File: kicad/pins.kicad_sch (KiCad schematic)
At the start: 2 parts, among them J1 Left, J2 Right

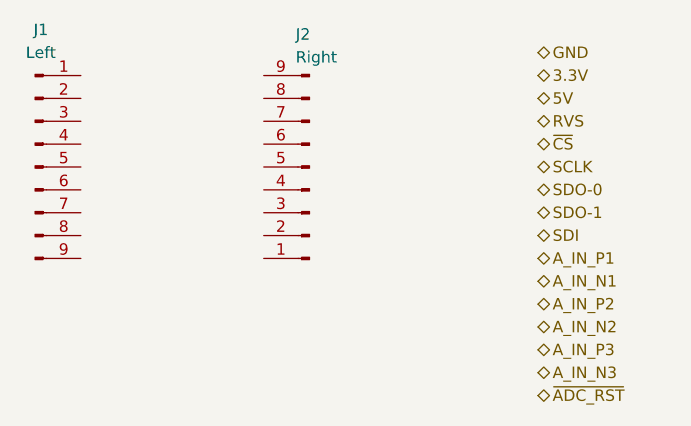
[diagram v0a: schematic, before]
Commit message: finish schematic for amp, and start routing (schematic isn't actually fully connected yet tho...)
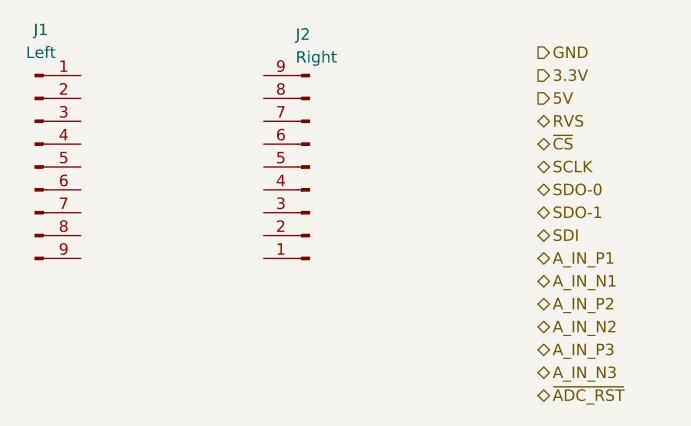
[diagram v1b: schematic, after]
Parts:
- J1, J2: footprint (none) -> Connector_PinHeader_1.00mm:PinHeader_1x09_P1.00mm_Horizontal
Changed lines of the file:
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@@
 	)
 	(hierarchical_label "5V"
-		(shape bidirectional)
+		(shape output)
 		(at 180.34 96.52 0)
 		(effects
@@
 	)
 	(hierarchical_label "GND"
-		(shape bidirectional)
+		(shape output)
 		(at 180.34 91.44 0)
 		(effects
@@
 	)
 	(hierarchical_label "3.3V"
-		(shape bidirectional)
+		(shape output)
 		(at 180.34 93.98 0)
 		(effects
@@
 			)
 		)
-		(property "Footprint" ""
+		(property "Footprint" "Connector_PinHeader_1.00mm:PinHeader_1x09_P1.00mm_Horizontal"
 			(at 154.94 104.14 0)
 			(effects
@@
 			)
 		)
-		(property "Footprint" ""
+		(property "Footprint" "Connector_PinHeader_1.00mm:PinHeader_1x09_P1.00mm_Horizontal"
 			(at 124.46 104.14 0)
 			(effects

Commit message: started routing pcb
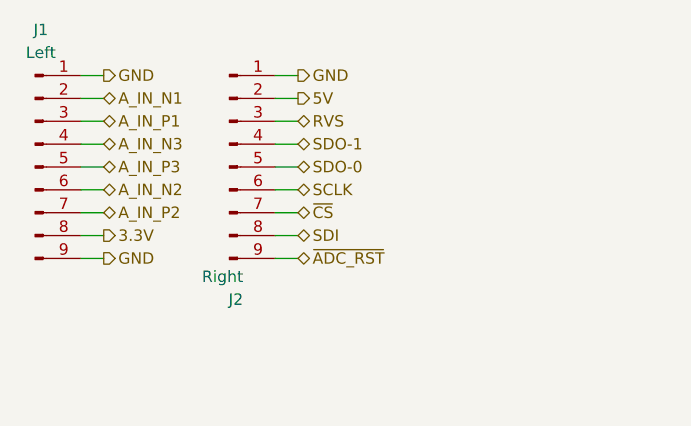
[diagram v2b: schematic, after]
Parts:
- J1, J2: footprint Connector_PinHeader_1.00mm:PinHeader_1x09_P1.00mm_Horizontal -> Connector_PinHeader_1.00mm:PinHeader_1x09_P1.00mm_Vertical
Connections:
- net 3.3V: now also J1.8 (Pin_8)
- net 5V: now also J2.2 (Pin_2)
- net A_IN_N1: now also J1.2 (Pin_2)
- net A_IN_N2: now also J1.6 (Pin_6)
- net A_IN_N3: now also J1.4 (Pin_4)
- net A_IN_P1: now also J1.3 (Pin_3)
- net A_IN_P2: now also J1.7 (Pin_7)
- net A_IN_P3: now also J1.5 (Pin_5)
- net GND: now also J1.1 (Pin_1), J1.9 (Pin_9), J2.1 (Pin_1)
- net RVS: now also J2.3 (Pin_3)
- net SCLK: now also J2.6 (Pin_6)
- net SDI: now also J2.8 (Pin_8)
- net SDO-0: now also J2.5 (Pin_5)
- net SDO-1: now also J2.4 (Pin_4)
- net ~{ADC_RST}: now also J2.9 (Pin_9)
- net ~{CS}: now also J2.7 (Pin_7)
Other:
- moved on the sheet: J2
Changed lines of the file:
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@@
 	(generator_version "9.0")
 	(paper "A4")
+	(wire
+		(pts
+			(xy 129.54 114.3) (xy 132.08 114.3)
+		)
+		(stroke
+			(width 0)
+			(type default)
+		)
+	)
+	(wire
+		(pts
+			(xy 151.13 104.14) (xy 153.67 104.14)
+		)
+		(stroke
+			(width 0)
+			(type default)
+		)
+	)
+	(wire
+		(pts
+			(xy 151.13 109.22) (xy 153.67 109.22)
+		)
+		(stroke
+			(width 0)
+			(type default)
+		)
+	)
+	(wire
+		(pts
+			(xy 129.54 99.06) (xy 132.08 99.06)
+		)
+		(stroke
+			(width 0)
+			(type default)
+		)
+	)
+	(wire
+		(pts
+			(xy 151.13 101.6) (xy 153.67 101.6)
+		)
+		(stroke
+			(width 0)
+			(type default)
+		)
+	)
+	(wire
+		(pts
+			(xy 151.13 93.98) (xy 153.67 93.98)
+		)
+		(stroke
+			(width 0)
+			(type default)
+		)
+	)
+	(wire
+		(pts
+			(xy 151.13 96.52) (xy 153.67 96.52)
+		)
+		(stroke
+			(width 0)
+			(type default)
+		)
+	)
+	(wire
+		(pts
+			(xy 151.13 114.3) (xy 153.67 114.3)
+		)
+		(stroke
+			(width 0)
+			(type default)
+		)
+	)
+	(wire
+		(pts
+			(xy 129.54 96.52) (xy 132.08 96.52)
+		)
+		(stroke
+			(width 0)
+			(type default)
+		)
+	)
+	(wire
+		(pts
+			(xy 151.13 99.06) (xy 153.67 99.06)
+		)
+		(stroke
+			(width 0)
+			(type default)
+		)
+	)
+	(wire
+		(pts
+			(xy 129.54 106.68) (xy 132.08 106.68)
+		)
+		(stroke
+			(width 0)
+			(type default)
+		)
+	)
+	(wire
+		(pts
+			(xy 129.54 101.6) (xy 132.08 101.6)
+		)
+		(stroke
+			(width 0)
+			(type default)
+		)
+	)
+	(wire
+		(pts
+			(xy 129.54 93.98) (xy 132.08 93.98)
+		)
+		(stroke
+			(width 0)
+			(type default)
+		)
+	)
+	(wire
+		(pts
+			(xy 129.54 109.22) (xy 132.08 109.22)
+		)
+		(stroke
+			(width 0)
+			(type default)
+		)
+	)
+	(wire
+		(pts
+			(xy 129.54 111.76) (xy 132.08 111.76)
+		)
+		(stroke
+			(width 0)
+			(type default)
+		)
+	)
+	(wire
+		(pts
+			(xy 151.13 111.76) (xy 153.67 111.76)
+		)
+		(stroke
+			(width 0)
+			(type default)
+		)
+	)
+	(wire
+		(pts
+			(xy 129.54 104.14) (xy 132.08 104.14)
+		)
+		(stroke
+			(width 0)
+			(type default)
+		)
+	)
+	(wire
+		(pts
+			(xy 151.13 106.68) (xy 153.67 106.68)
+		)
+		(stroke
+			(width 0)
+			(type default)
+		)
+	)
 	(hierarchical_label "A_IN_P2"
 		(shape bidirectional)
-		(at 180.34 119.38 0)
+		(at 132.08 109.22 0)
 		(effects
 			(font
@@
 	(hierarchical_label "SDO-0"
 		(shape bidirectional)
-		(at 180.34 106.68 0)
+		(at 153.67 104.14 0)
 		(effects
 			(font
@@
 	(hierarchical_label "~{ADC_RST}"
 		(shape bidirectional)
-		(at 180.34 129.54 0)
+		(at 153.67 114.3 0)
 		(effects
 			(font
@@
 	(hierarchical_label "SDI"
 		(shape bidirectional)
-		(at 180.34 111.76 0)
+		(at 153.67 111.76 0)
 		(effects
 			(font
@@
 	(hierarchical_label "5V"
 		(shape output)
-		(at 180.34 96.52 0)
-		(effects
-			(font
-				(size 1.27 1.27)
-			)
-			(justify left)
-		)
-	)
-	(hierarchical_label "A_IN_N2"
-		(shape bidirectional)
-		(at 180.34 121.92 0)
-		(effects
-			(font
-				(size 1.27 1.27)
-			)
-			(justify left)
-		)
-	)
-	(hierarchical_label "A_IN_N1"
-		(shape bidirectional)
-		(at 180.34 116.84 0)
-		(effects
-			(font
-				(size 1.27 1.27)
-			)
-			(justify left)
-		)
-	)
-	(hierarchical_label "SDO-1"
-		(shape bidirectional)
-		(at 180.34 109.22 0)
+		(at 153.67 96.52 0)
 		(effects
 			(font
@@
 	(hierarchical_label "GND"
 		(shape output)
-		(at 180.34 91.44 0)
+		(at 132.08 114.3 0)
+		(effects
+			(font
+				(size 1.27 1.27)
+			)
+			(justify left)
+		)
+	)
+	(hierarchical_label "A_IN_N2"
+		(shape bidirectional)
+		(at 132.08 106.68 0)
+		(effects
+			(font
+				(size 1.27 1.27)
+			)
+			(justify left)
+		)
+	)
+	(hierarchical_label "A_IN_N1"
+		(shape bidirectional)
+		(at 132.08 96.52 0)
+		(effects
+			(font
+				(size 1.27 1.27)
+			)
+			(justify left)
+		)
+	)
+	(hierarchical_label "SDO-1"
+		(shape bidirectional)
+		(at 153.67 101.6 0)
+		(effects
+			(font
+				(size 1.27 1.27)
+			)
+			(justify left)
+		)
+	)
+	(hierarchical_label "GND"
+		(shape output)
+		(at 153.67 93.98 0)
+		(effects
+			(font
+				(size 1.27 1.27)
+			)
+			(justify left)
+		)
+	)
+	(hierarchical_label "GND"
+		(shape output)
+		(at 132.08 93.98 0)
 		(effects
 			(font
@@
 	(hierarchical_label "SCLK"
 		(shape bidirectional)
-		(at 180.34 104.14 0)
+		(at 153.67 106.68 0)
 		(effects
 			(font
@@
 	(hierarchical_label "~{CS}"
 		(shape bidirectional)
-		(at 180.34 101.6 0)
+		(at 153.67 109.22 0)
 		(effects
 			(font
@@
 	(hierarchical_label "A_IN_P1"
 		(shape bidirectional)
-		(at 180.34 114.3 0)
+		(at 132.08 99.06 0)
 		(effects
 			(font
@@
 	(hierarchical_label "RVS"
 		(shape bidirectional)
-		(at 180.34 99.06 0)
+		(at 153.67 99.06 0)
 		(effects
 			(font
@@
 	(hierarchical_label "A_IN_P3"
 		(shape bidirectional)
-		(at 180.34 124.46 0)
+		(at 132.08 104.14 0)
 		(effects
 			(font
@@
 	(hierarchical_label "A_IN_N3"
 		(shape bidirectional)
-		(at 180.34 127 0)
+		(at 132.08 101.6 0)
 		(effects
 			(font
@@
 	(hierarchical_label "3.3V"
 		(shape output)
-		(at 180.34 93.98 0)
+		(at 132.08 111.76 0)
 		(effects
 			(font
@@
 	(symbol
 		(lib_id "Connector:Conn_01x09_Pin")
-		(at 154.94 104.14 180)
+		(at 146.05 104.14 0)
 		(unit 1)
 		(exclude_from_sim no)
@@
 		(dnp no)
 		(property "Reference" "J2"
-			(at 153.416 89.408 0)
+			(at 147.574 118.872 0)
 			(effects
 				(font
@@
 		)
 		(property "Value" "Right"
-			(at 153.416 91.948 0)
+			(at 147.574 116.332 0)
 			(effects
 				(font
@@
 			)
 		)
-		(property "Footprint" "Connector_PinHeader_1.00mm:PinHeader_1x09_P1.00mm_Horizontal"
-			(at 154.94 104.14 0)
+		(property "Footprint" "Connector_PinHeader_1.00mm:PinHeader_1x09_P1.00mm_Vertical"
+			(at 146.05 104.14 0)
 			(effects
 				(font
@@
 		)
 		(property "Datasheet" "~"
-			(at 154.94 104.14 0)
+			(at 146.05 104.14 0)
 			(effects
 				(font
@@
 		)
 		(property "Description" "Generic connector, single row, 01x09, script generated"
-			(at 154.94 104.14 0)
+			(at 146.05 104.14 0)
 			(effects
 				(font
@@
 			)
 		)
-		(property "Footprint" "Connector_PinHeader_1.00mm:PinHeader_1x09_P1.00mm_Horizontal"
+		(property "Footprint" "Connector_PinHeader_1.00mm:PinHeader_1x09_P1.00mm_Vertical"
 			(at 124.46 104.14 0)
 			(effects

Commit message: redo routing with correct header pin footprint
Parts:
- J1, J2: footprint Connector_PinHeader_1.00mm:PinHeader_1x09_P1.00mm_Vertical -> Connector_PinHeader_2.54mm:PinHeader_1x09_P2.54mm_Vertical
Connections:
- net RVS: now also J2.9 (Pin_9); no longer J2.3 (Pin_3)
- net SDI: now also J2.4 (Pin_4); no longer J2.8 (Pin_8)
- net SDO-0: now also J2.7 (Pin_7); no longer J2.5 (Pin_5)
- net SDO-1: now also J2.8 (Pin_8); no longer J2.4 (Pin_4)
- net ~{ADC_RST}: now also J2.3 (Pin_3); no longer J2.9 (Pin_9)
- net ~{CS}: now also J2.5 (Pin_5); no longer J2.7 (Pin_7)
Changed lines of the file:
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@@
 	(hierarchical_label "SDO-0"
 		(shape bidirectional)
+		(at 153.67 109.22 0)
+		(effects
+			(font
+				(size 1.27 1.27)
+			)
+			(justify left)
+		)
+	)
+	(hierarchical_label "~{ADC_RST}"
+		(shape bidirectional)
+		(at 153.67 99.06 0)
+		(effects
+			(font
+				(size 1.27 1.27)
+			)
+			(justify left)
+		)
+	)
+	(hierarchical_label "SDI"
+		(shape bidirectional)
+		(at 153.67 101.6 0)
+		(effects
+			(font
+				(size 1.27 1.27)
+			)
+			(justify left)
+		)
+	)
+	(hierarchical_label "5V"
+		(shape output)
+		(at 153.67 96.52 0)
+		(effects
+			(font
+				(size 1.27 1.27)
+			)
+			(justify left)
+		)
+	)
+	(hierarchical_label "GND"
+		(shape output)
+		(at 132.08 114.3 0)
+		(effects
+			(font
+				(size 1.27 1.27)
+			)
+			(justify left)
+		)
+	)
+	(hierarchical_label "A_IN_N2"
+		(shape bidirectional)
+		(at 132.08 106.68 0)
+		(effects
+			(font
+				(size 1.27 1.27)
+			)
+			(justify left)
+		)
+	)
+	(hierarchical_label "A_IN_N1"
+		(shape bidirectional)
+		(at 132.08 96.52 0)
+		(effects
+			(font
+				(size 1.27 1.27)
+			)
+			(justify left)
+		)
+	)
+	(hierarchical_label "SDO-1"
+		(shape bidirectional)
+		(at 153.67 111.76 0)
+		(effects
+			(font
+				(size 1.27 1.27)
+			)
+			(justify left)
+		)
+	)
+	(hierarchical_label "GND"
+		(shape output)
+		(at 153.67 93.98 0)
+		(effects
+			(font
+				(size 1.27 1.27)
+			)
+			(justify left)
+		)
+	)
+	(hierarchical_label "GND"
+		(shape output)
+		(at 132.08 93.98 0)
+		(effects
+			(font
+				(size 1.27 1.27)
+			)
+			(justify left)
+		)
+	)
+	(hierarchical_label "SCLK"
+		(shape bidirectional)
+		(at 153.67 106.68 0)
+		(effects
+			(font
+				(size 1.27 1.27)
+			)
+			(justify left)
+		)
+	)
+	(hierarchical_label "~{CS}"
+		(shape bidirectional)
 		(at 153.67 104.14 0)
 		(effects
@@
 		)
 	)
-	(hierarchical_label "~{ADC_RST}"
+	(hierarchical_label "A_IN_P1"
+		(shape bidirectional)
+		(at 132.08 99.06 0)
+		(effects
+			(font
+				(size 1.27 1.27)
+			)
+			(justify left)
+		)
+	)
+	(hierarchical_label "RVS"
 		(shape bidirectional)
 		(at 153.67 114.3 0)
-		(effects
-			(font
-				(size 1.27 1.27)
-			)
-			(justify left)
-		)
-	)
-	(hierarchical_label "SDI"
-		(shape bidirectional)
-		(at 153.67 111.76 0)
-		(effects
-			(font
-				(size 1.27 1.27)
-			)
-			(justify left)
-		)
-	)
-	(hierarchical_label "5V"
-		(shape output)
-		(at 153.67 96.52 0)
-		(effects
-			(font
-				(size 1.27 1.27)
-			)
-			(justify left)
-		)
-	)
-	(hierarchical_label "GND"
-		(shape output)
-		(at 132.08 114.3 0)
-		(effects
-			(font
-				(size 1.27 1.27)
-			)
-			(justify left)
-		)
-	)
-	(hierarchical_label "A_IN_N2"
-		(shape bidirectional)
-		(at 132.08 106.68 0)
-		(effects
-			(font
-				(size 1.27 1.27)
-			)
-			(justify left)
-		)
-	)
-	(hierarchical_label "A_IN_N1"
-		(shape bidirectional)
-		(at 132.08 96.52 0)
-		(effects
-			(font
-				(size 1.27 1.27)
-			)
-			(justify left)
-		)
-	)
-	(hierarchical_label "SDO-1"
-		(shape bidirectional)
-		(at 153.67 101.6 0)
-		(effects
-			(font
-				(size 1.27 1.27)
-			)
-			(justify left)
-		)
-	)
-	(hierarchical_label "GND"
-		(shape output)
-		(at 153.67 93.98 0)
-		(effects
-			(font
-				(size 1.27 1.27)
-			)
-			(justify left)
-		)
-	)
-	(hierarchical_label "GND"
-		(shape output)
-		(at 132.08 93.98 0)
-		(effects
-			(font
-				(size 1.27 1.27)
-			)
-			(justify left)
-		)
-	)
-	(hierarchical_label "SCLK"
-		(shape bidirectional)
-		(at 153.67 106.68 0)
-		(effects
-			(font
-				(size 1.27 1.27)
-			)
-			(justify left)
-		)
-	)
-	(hierarchical_label "~{CS}"
-		(shape bidirectional)
-		(at 153.67 109.22 0)
-		(effects
-			(font
-				(size 1.27 1.27)
-			)
-			(justify left)
-		)
-	)
-	(hierarchical_label "A_IN_P1"
-		(shape bidirectional)
-		(at 132.08 99.06 0)
-		(effects
-			(font
-				(size 1.27 1.27)
-			)
-			(justify left)
-		)
-	)
-	(hierarchical_label "RVS"
-		(shape bidirectional)
-		(at 153.67 99.06 0)
 		(effects
 			(font
@@
 			)
 		)
-		(property "Footprint" "Connector_PinHeader_1.00mm:PinHeader_1x09_P1.00mm_Vertical"
+		(property "Footprint" "Connector_PinHeader_2.54mm:PinHeader_1x09_P2.54mm_Vertical"
 			(at 146.05 104.14 0)
 			(effects
@@
 			)
 		)
-		(property "Footprint" "Connector_PinHeader_1.00mm:PinHeader_1x09_P1.00mm_Vertical"
+		(property "Footprint" "Connector_PinHeader_2.54mm:PinHeader_1x09_P2.54mm_Vertical"
 			(at 124.46 104.14 0)
 			(effects
